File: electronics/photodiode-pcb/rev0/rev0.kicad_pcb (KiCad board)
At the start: 2 copper layers, 90 x 12 mm, 20 parts, among them IC1 AS89010, IC2 AS89010, J1 Conn_01x08_Male

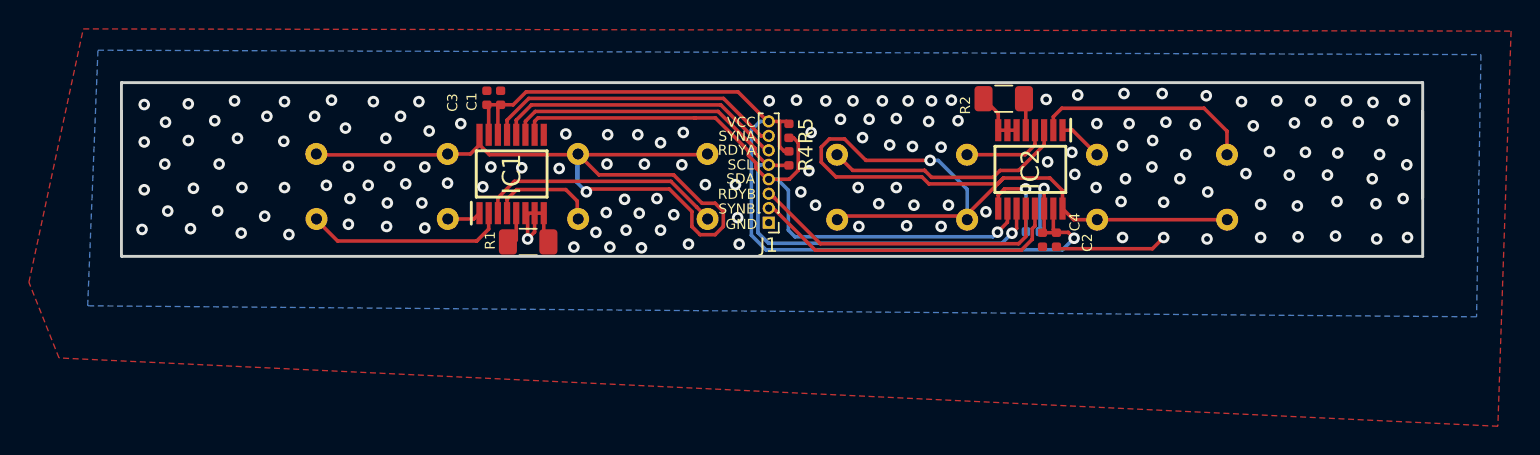
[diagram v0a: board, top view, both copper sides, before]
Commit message: updating README. fixing edge_cuts in emmision pcb.
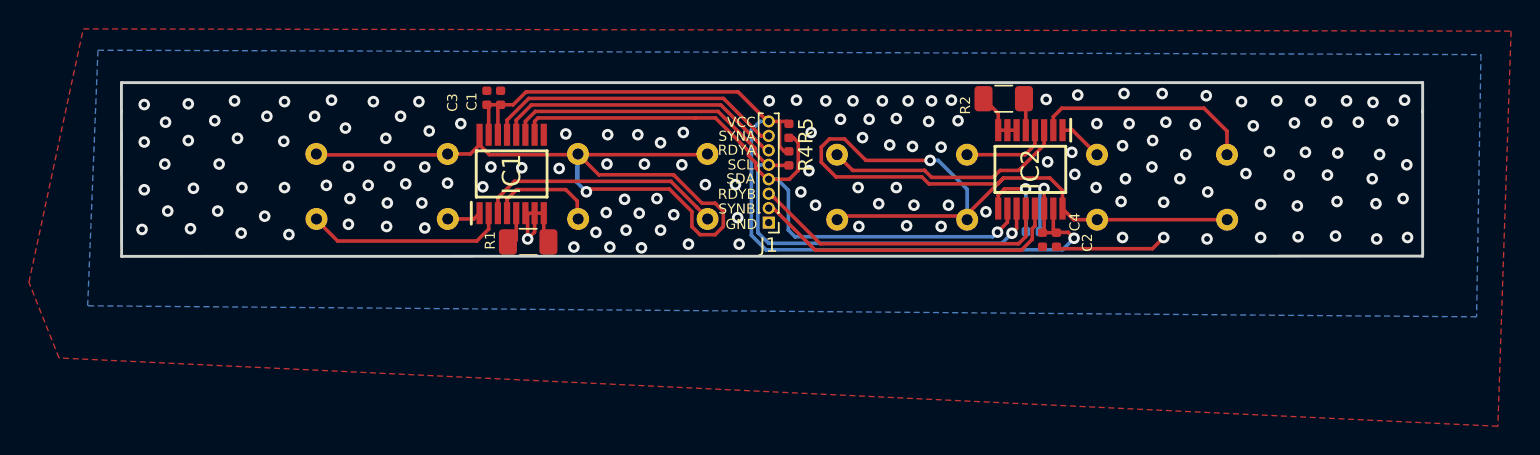
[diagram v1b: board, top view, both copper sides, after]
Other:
- outline, holes or cut-outs redrawn
